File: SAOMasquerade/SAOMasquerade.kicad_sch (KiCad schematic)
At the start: 20 parts, among them Q1 BSS138, SW1 SW_DIP_x07, U1 CH32V003FxPx, U2 74LVC1G86, U3 74LVC1G38, X1 SAO, X2 BADGE

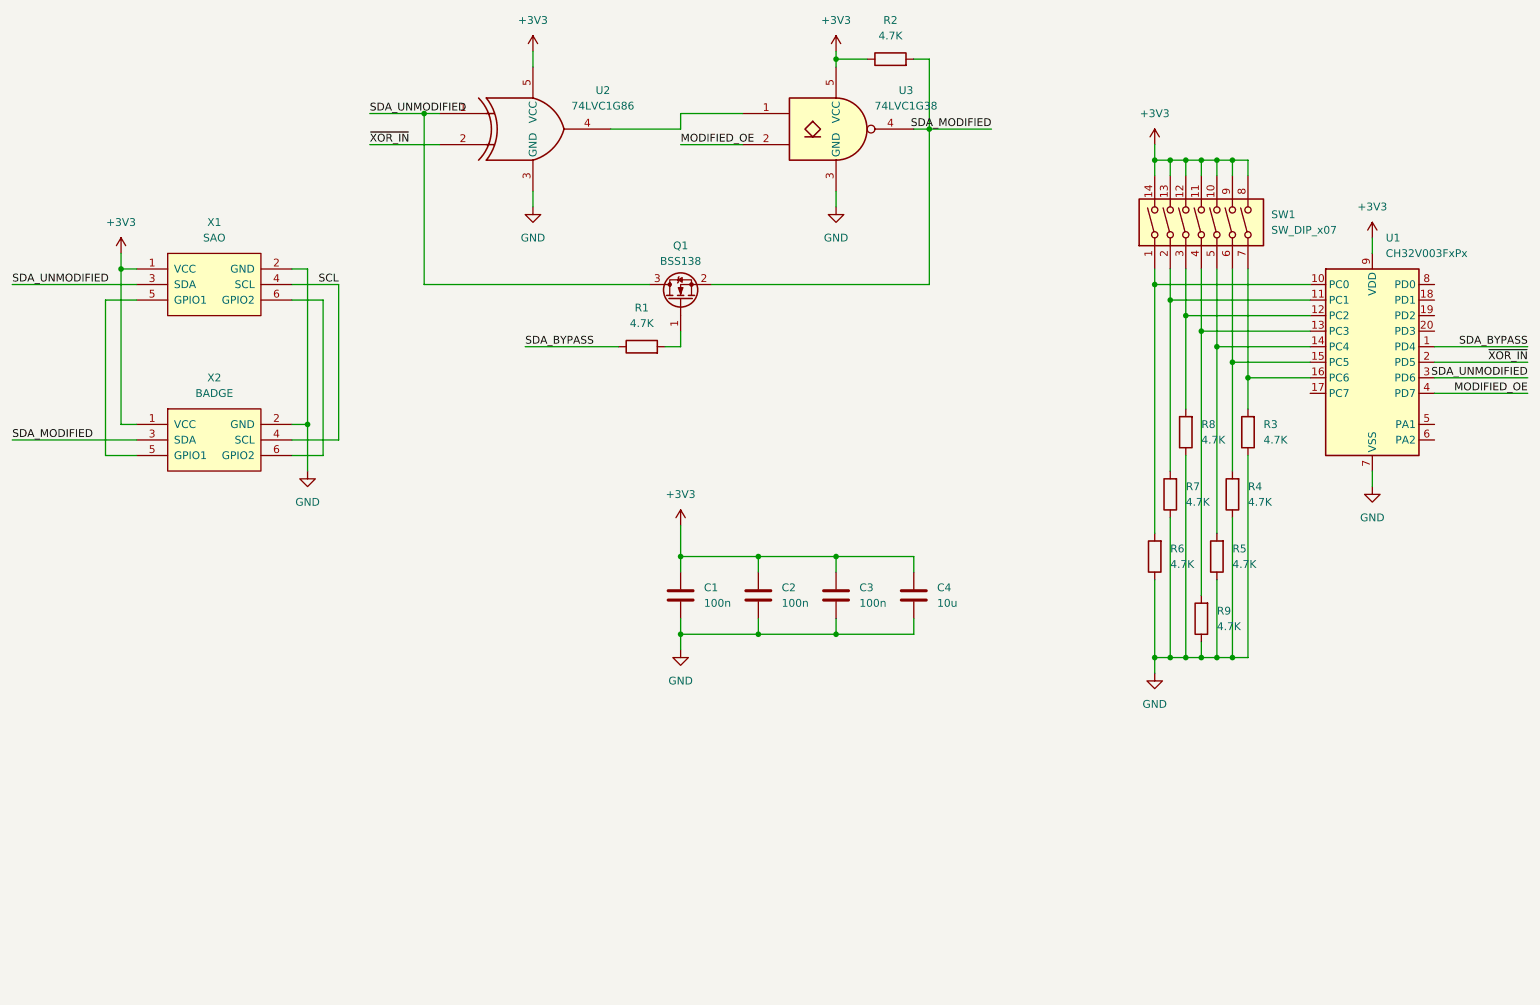
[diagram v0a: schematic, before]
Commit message: Updating schematic to use analog switch instead of open drain NAND
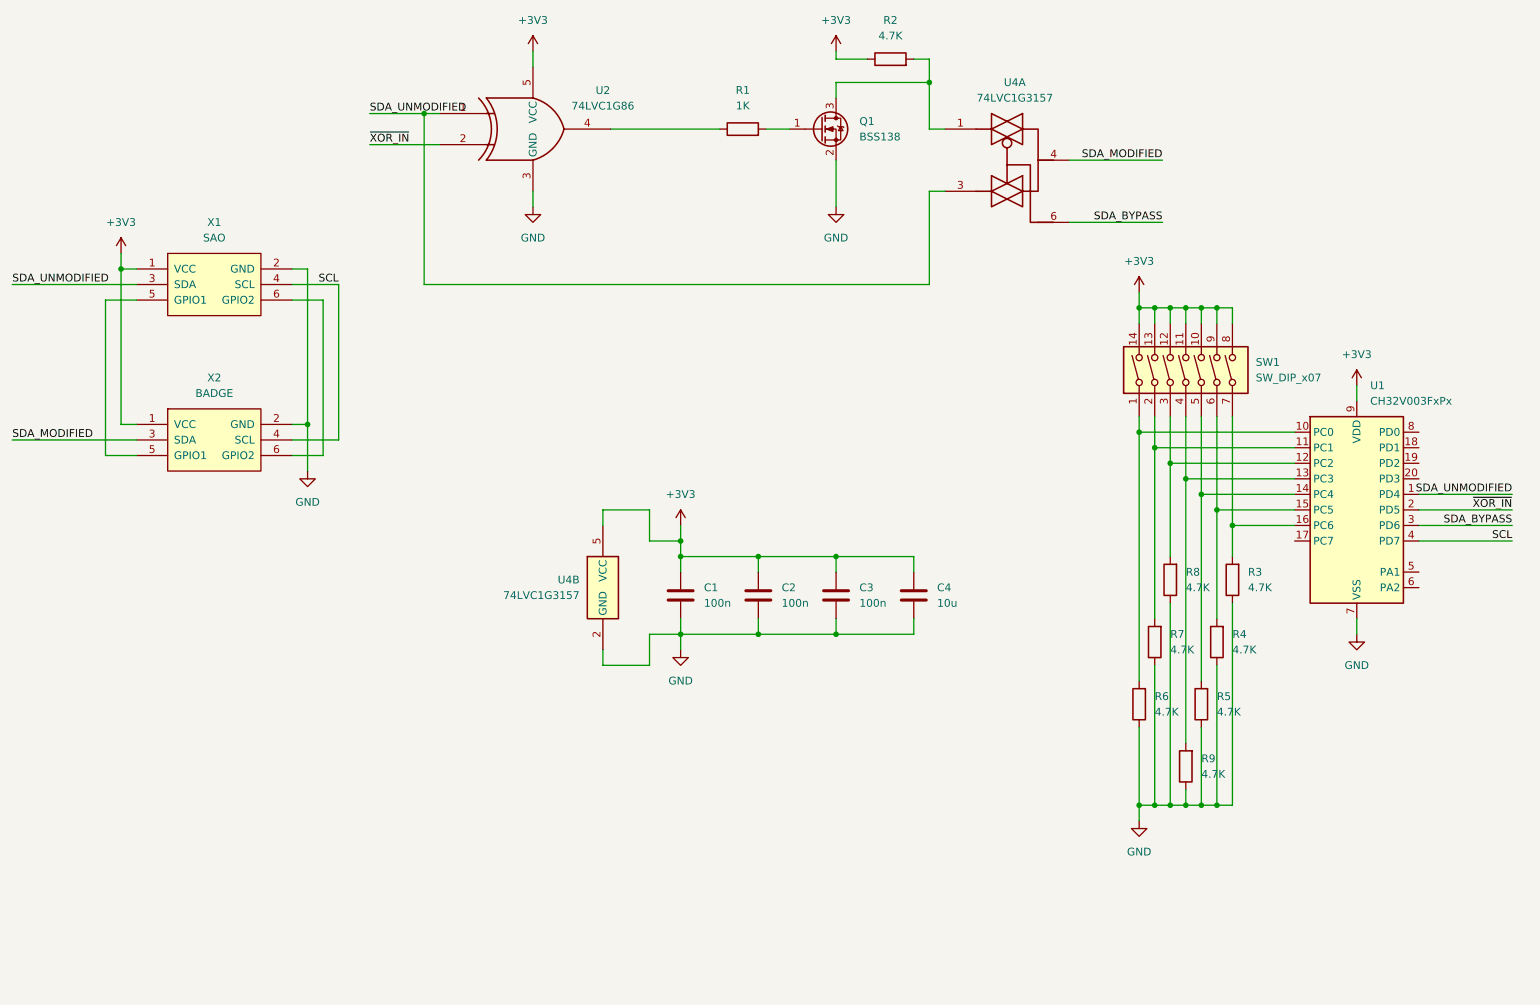
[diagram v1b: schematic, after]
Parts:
- removed U3: 74LVC1G38, Package_TO_SOT_SMD:SOT-23-5, symbol 74xGxx:74LVC1G38
- added U4: 74LVC1G3157, Package_TO_SOT_SMD:SOT-23-6_Handsoldering, symbol 74xGxx:74LVC1G3157
- Q1: footprint Package_TO_SOT_SMD:SOT-23 -> Package_TO_SOT_SMD:SOT-23_Handsoldering
- R1: value 4.7K -> 1K
- U2: footprint Package_TO_SOT_SMD:SOT-23-5 -> Package_TO_SOT_SMD:SOT-23-5_HandSoldering
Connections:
- net MODIFIED_OE is gone; now on net SCL: U1.4 (PD7)
- net +3V3: now also U4.5 (VCC)
- net GND: now also Q1.2 (S), U4.2 (GND)
- net SDA_BYPASS: now also U1.3 (PD6), U4.6; no longer R1.1, U1.1 (PD4)
- net SDA_MODIFIED: now also U4.4; no longer Q1.2 (S), R2.2
- net SDA_UNMODIFIED: now also U1.1 (PD4), U4.3; no longer Q1.3 (D), U1.3 (PD6)
- net at U2.4: now also R1.1
- new net: Q1.3 (D), R2.2, U4.1
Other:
- moved on the sheet: R3, R4, R5, R6, R7, R8, R9, SW1, U1

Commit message: Adding debuggability
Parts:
- added J1: Conn_01x04, Connector_PinHeader_2.54mm:PinHeader_1x04_P2.54mm_Vertical, symbol Connector_Generic:Conn_01x04
- added J2: Conn_01x03, Connector_PinHeader_2.54mm:PinHeader_1x03_P2.54mm_Vertical, symbol Connector_Generic:Conn_01x03
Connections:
- net +3V3: now also J1.1 (Pin_1)
- net GND: now also J1.4 (Pin_4), J2.3 (Pin_3)
- net SCL: now also U1.5 (PA1); no longer U1.4 (PD7)
- net SDA_BYPASS: now also U1.20 (PD3); no longer U1.3 (PD6)
- net SDA_UNMODIFIED: now also U1.19 (PD2); no longer U1.1 (PD4)
- net ~{XOR_IN}: now also U1.17 (PC7); no longer U1.2 (PD5)
- net SWIO: now reaches U1.18 (PD1)
- net SWIO: now also J1.2 (Pin_2)
- new net UART_RX: J2.2 (Pin_2), U1.3 (PD6)
- new net UART_TX: J2.1 (Pin_1), U1.2 (PD5)
- new net ~{RESET}: J1.3 (Pin_3), U1.4 (PD7)
